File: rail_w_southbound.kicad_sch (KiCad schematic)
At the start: 54 parts

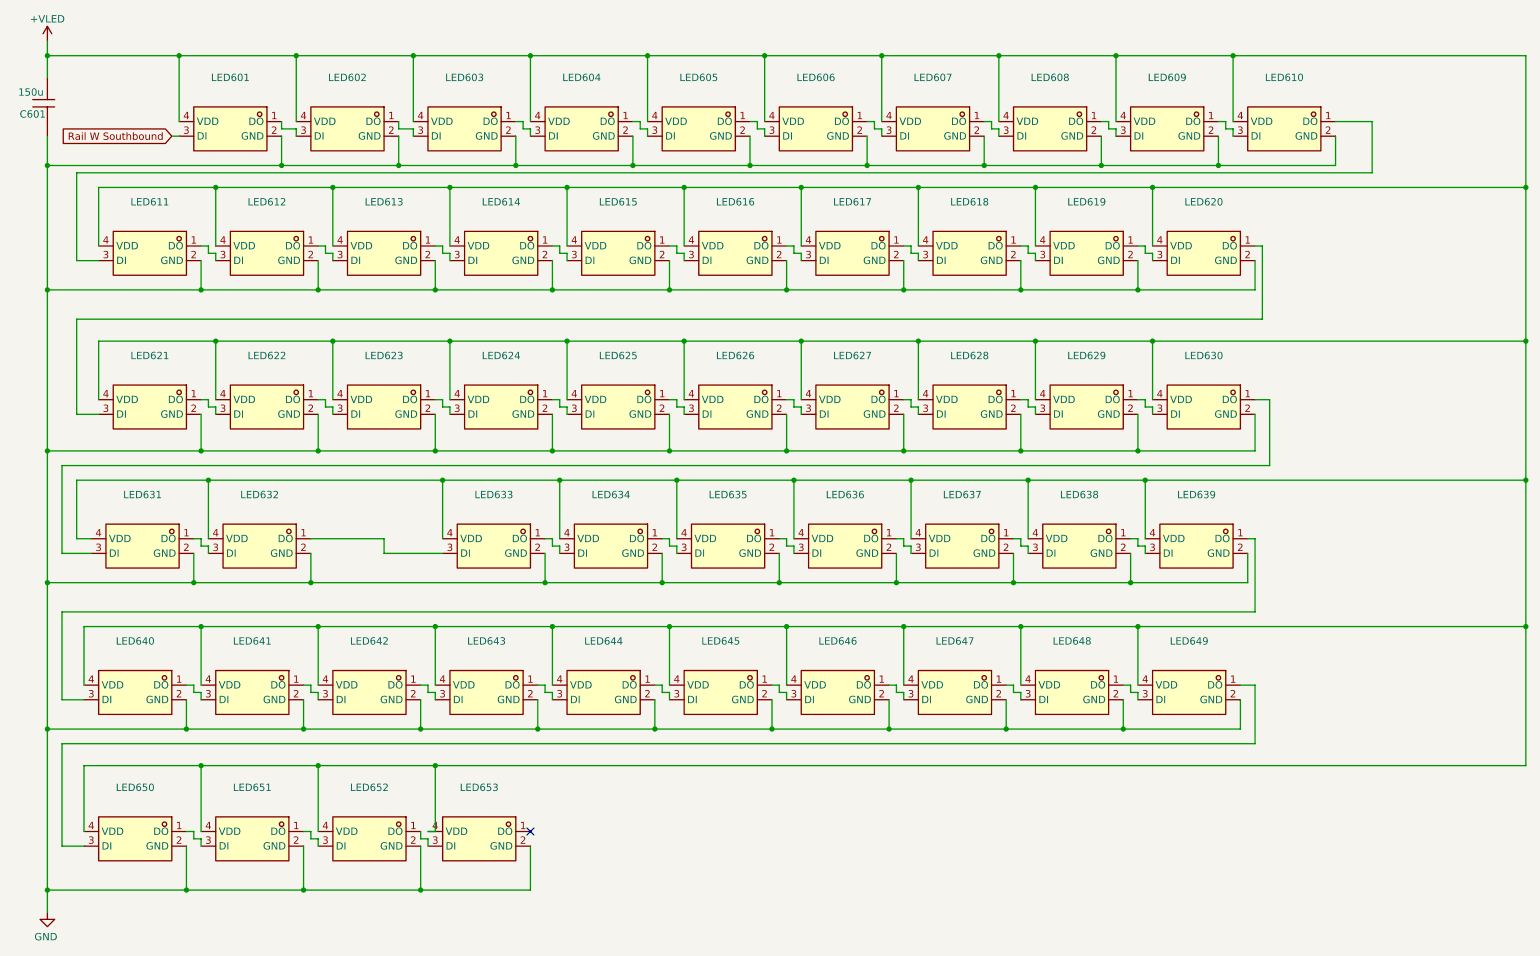
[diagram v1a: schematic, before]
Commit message: Add rail labels
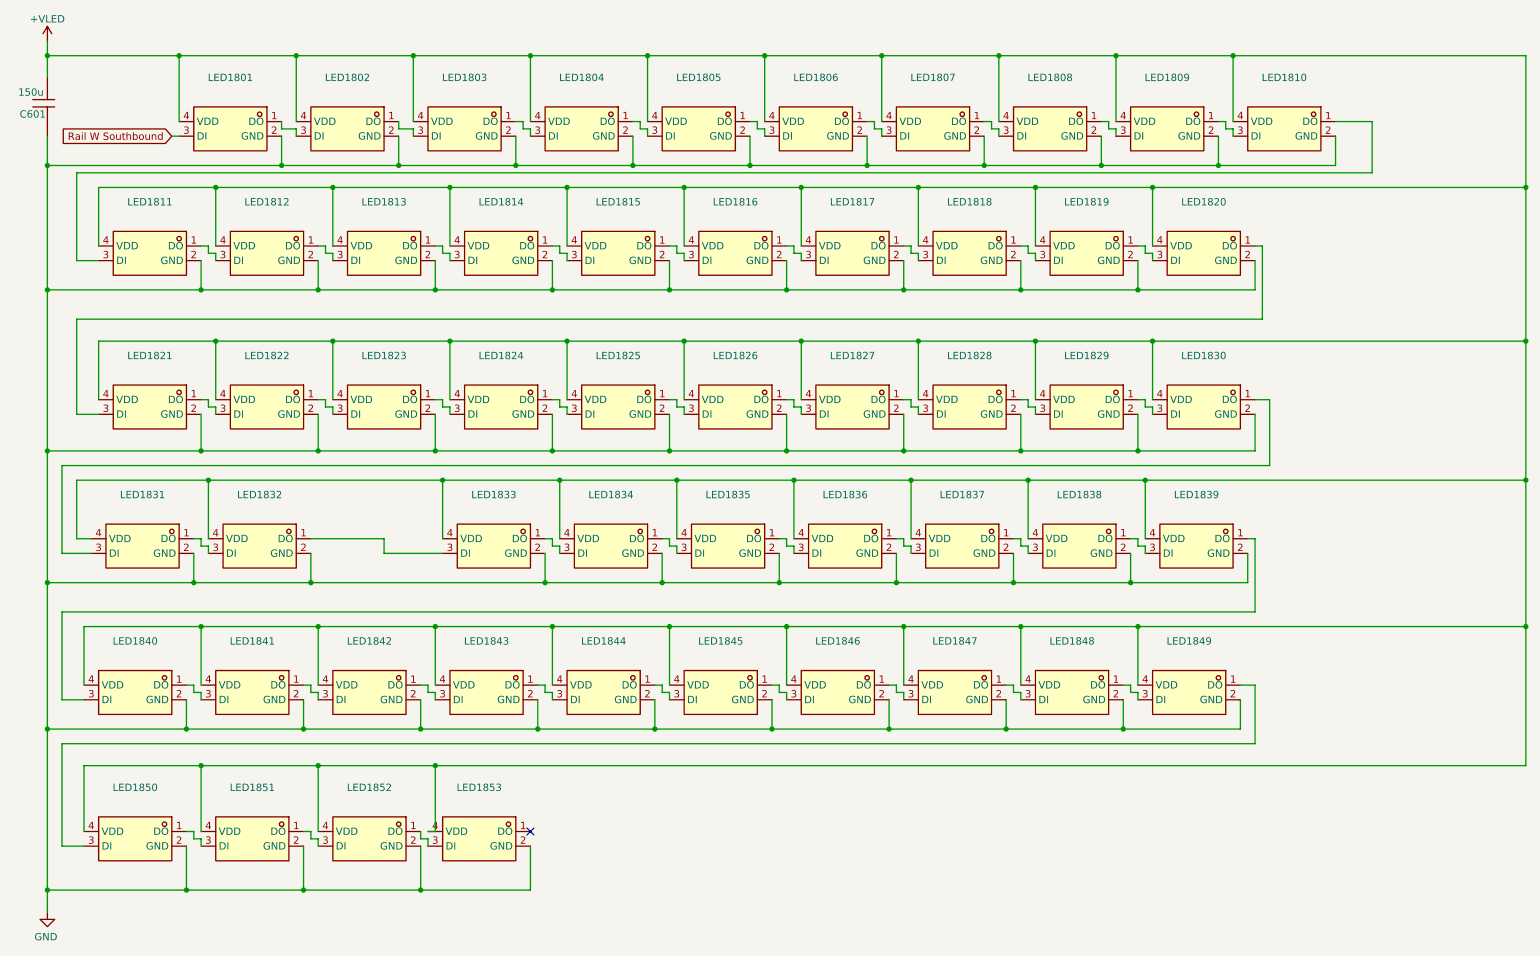
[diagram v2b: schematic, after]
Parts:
- renumbered LED601 to LED1801, LED602 to LED1802, LED603 to LED1803, LED604 to LED1804, LED605 to LED1805, LED606 to LED1806, LED607 to LED1807, LED608 to LED1808, LED609 to LED1809, LED610 to LED1810, LED611 to LED1811, LED612 to LED1812, LED613 to LED1813, LED614 to LED1814, LED615 to LED1815, LED616 to LED1816, LED617 to LED1817, LED618 to LED1818, LED619 to LED1819, LED620 to LED1820, LED621 to LED1821, LED622 to LED1822, LED623 to LED1823, LED624 to LED1824, LED625 to LED1825, LED626 to LED1826, LED627 to LED1827, LED628 to LED1828, LED629 to LED1829, LED630 to LED1830, LED631 to LED1831, LED632 to LED1832, LED633 to LED1833, LED634 to LED1834, LED635 to LED1835, LED636 to LED1836, LED637 to LED1837, LED638 to LED1838, LED639 to LED1839, LED640 to LED1840, LED641 to LED1841, LED642 to LED1842, LED643 to LED1843, LED644 to LED1844, LED645 to LED1845, LED646 to LED1846, LED647 to LED1847, LED648 to LED1848, LED649 to LED1849, LED650 to LED1850, LED651 to LED1851, LED652 to LED1852, LED653 to LED1853

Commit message: route T
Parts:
- renumbered LED1801 to LED1601, LED1802 to LED1602, LED1803 to LED1603, LED1804 to LED1604, LED1805 to LED1605, LED1806 to LED1606, LED1807 to LED1607, LED1808 to LED1608, LED1809 to LED1609, LED1810 to LED1610, LED1811 to LED1611, LED1812 to LED1612, LED1813 to LED1613, LED1814 to LED1614, LED1815 to LED1615, LED1816 to LED1616, LED1817 to LED1617, LED1818 to LED1618, LED1819 to LED1619, LED1820 to LED1620, LED1821 to LED1621, LED1822 to LED1622, LED1823 to LED1623, LED1824 to LED1624, LED1825 to LED1625, LED1826 to LED1626, LED1827 to LED1627, LED1828 to LED1628, LED1829 to LED1629, LED1830 to LED1630, LED1831 to LED1631, LED1832 to LED1632, LED1833 to LED1633, LED1834 to LED1634, LED1835 to LED1635, LED1836 to LED1636, LED1837 to LED1637, LED1838 to LED1638, LED1839 to LED1639, LED1840 to LED1640, LED1841 to LED1641, LED1842 to LED1642, LED1843 to LED1643, LED1844 to LED1644, LED1845 to LED1645, LED1846 to LED1646, LED1847 to LED1647, LED1848 to LED1648, LED1849 to LED1649, LED1850 to LED1650, LED1851 to LED1651, LED1852 to LED1652, LED1853 to LED1653

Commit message: route link 1
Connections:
- net LINK_1_2: now reaches LED1627.1 (DO)
- net LINK_1_2: no longer LED1628.3 (DI)
- net Rail W Southbound renamed LINK_1_S
- new net LINK_2_1: LED1628.3 (DI)
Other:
- moved on the sheet: LED1628, LED1629, LED1630

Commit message: rev-b validation run
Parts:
- removed C601: 150u, EasyEDA:CAP-SMD_L3.5-W2.8, symbol EasyEDA:CL21B106KOQNNNE
- LED1601, LED1602, LED1603, LED1604, LED1605, LED1606, LED1607, LED1608, LED1609, LED1610, LED1611, LED1612, LED1613, LED1614, LED1615, LED1616, LED1617, LED1618, LED1619, LED1620, LED1621, LED1622, LED1623, LED1624, LED1625, LED1626, LED1627, LED1628, LED1629, LED1630, LED1631, LED1632, LED1633, LED1634, LED1635, LED1636, LED1637, LED1638, LED1639, LED1640, LED1641, LED1642, LED1643, LED1644, LED1645, LED1646, LED1647, LED1648, LED1649, LED1650, LED1651, LED1652, LED1653: LCSC Part C965555 -> C52917434
